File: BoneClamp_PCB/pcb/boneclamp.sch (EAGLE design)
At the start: 4 parts, among them U1 AD7656YSTZ, U2 AD5754RBREZ, U3 SN74ABT541BDW

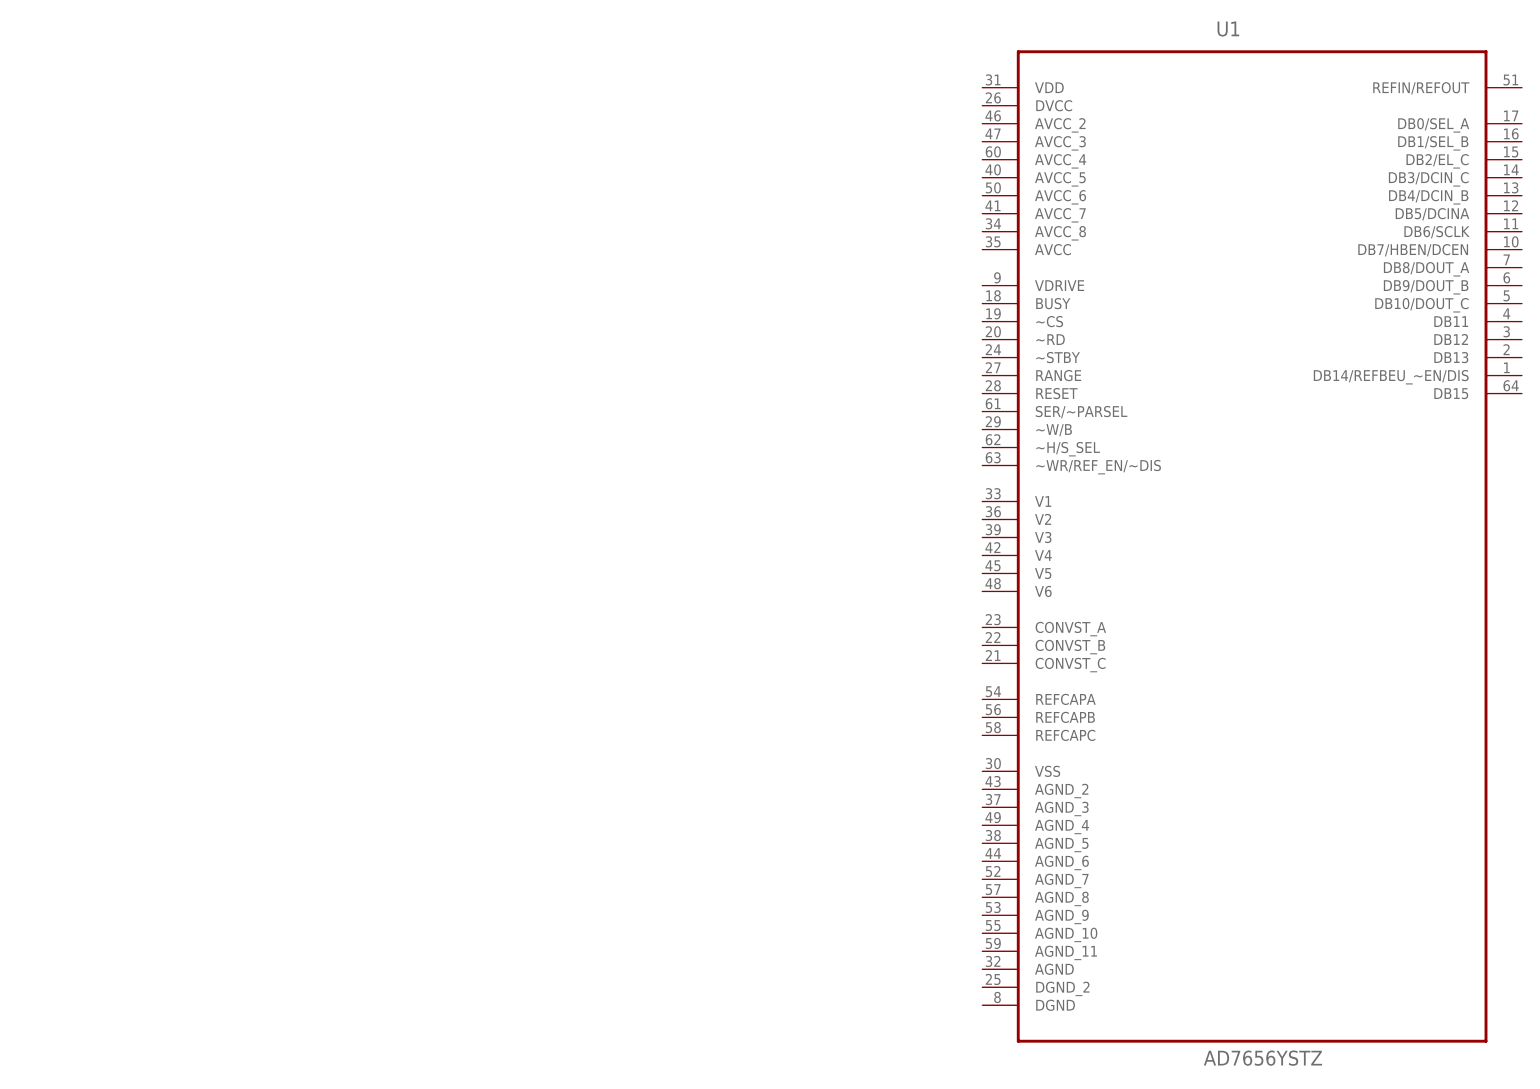
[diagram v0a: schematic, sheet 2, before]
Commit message: Updated schematic with the TRS jacks that we will use. They are mono which makes conversion to BNC or other formats easy. Also, I added a .gitignore to the main BoneClamp folder so that we can avoid committing executables and backup files.
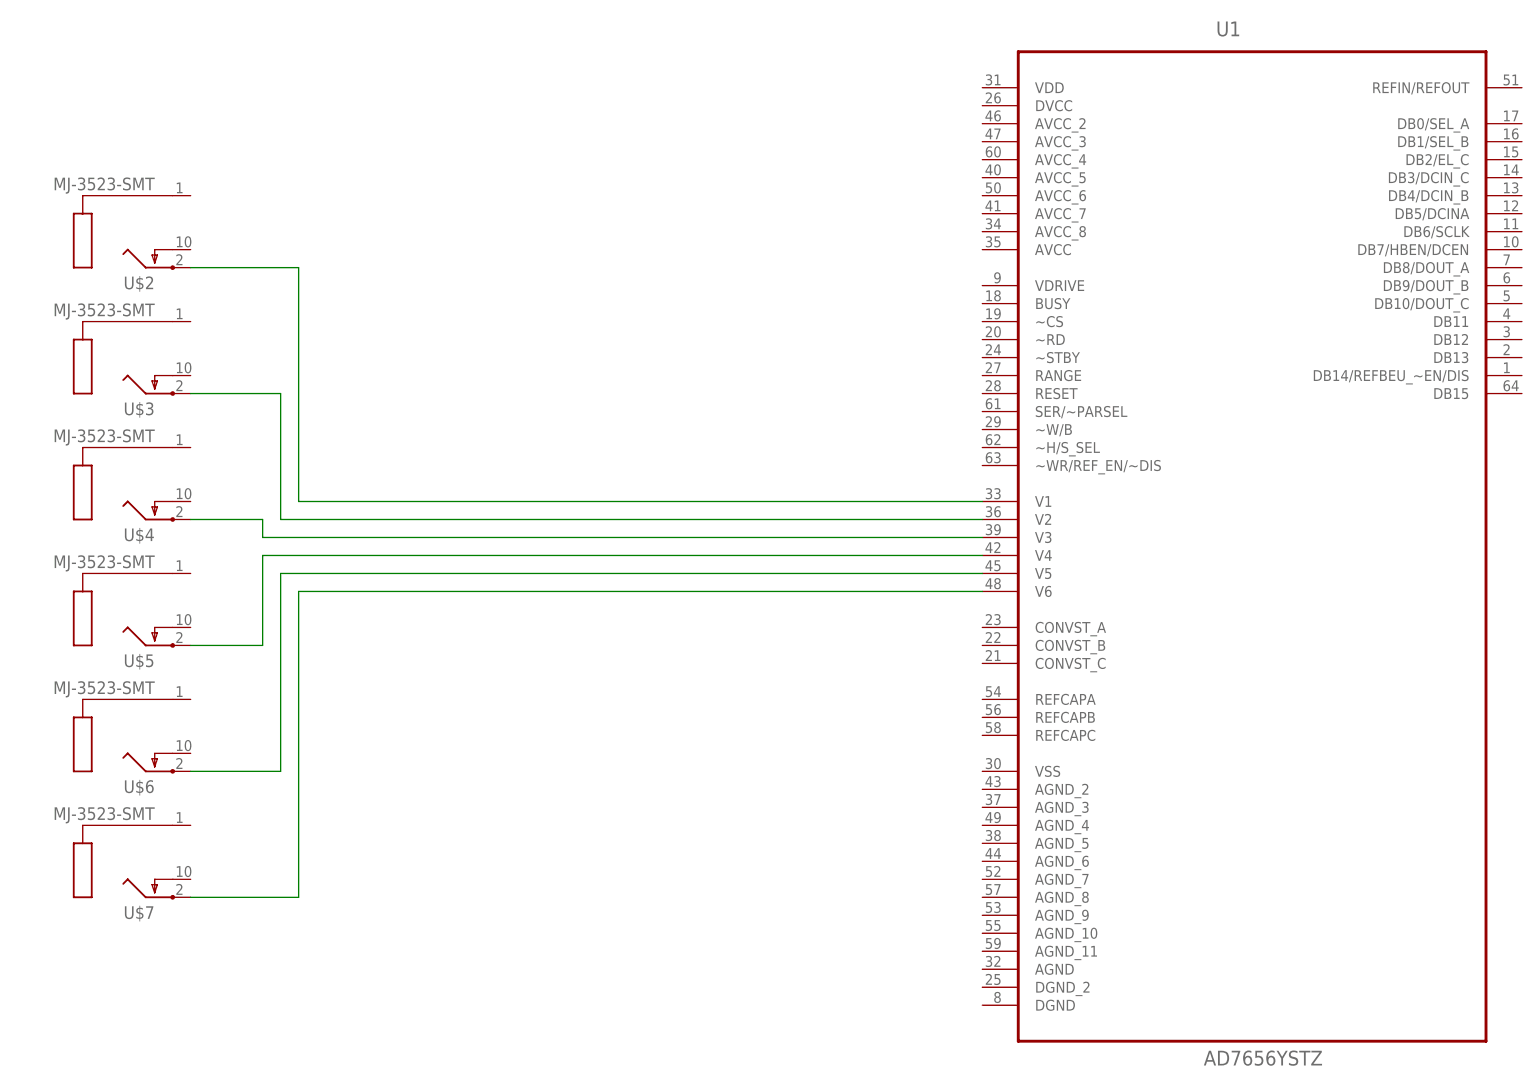
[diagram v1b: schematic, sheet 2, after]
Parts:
- added U$10, U$11, U$12, U$2, U$3, U$4, U$5, U$6, U$7, U$8: MJ-3523-SMT, con-cuistack:MJ-3523-SMT
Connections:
- new net N$1: U$6.TIP, U1.V5
- new net N$11: U$12.TIP, U2.VOUTD
- new net N$2: U$7.TIP, U1.V6
- new net N$3: U$5.TIP, U1.V4
- new net N$4: U$4.TIP, U1.V3
- new net N$5: U$3.TIP, U1.V2
- new net N$6: U$2.TIP, U1.V1
- new net N$7: U$8.TIP, U2.VOUTA
- new net N$8: U$10.TIP, U2.VOUTB
- new net N$9: U$11.TIP, U2.VOUTC
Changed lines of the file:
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@@
 <part name="U2" library="analog-devices-01" deviceset="AD5754RBREZ" device=""/>
 <part name="U3" library="ti-extended" deviceset="SN74ABT541BDW" device=""/>
+<part name="U$2" library="con-cuistack" deviceset="MJ-3523-SMT" device=""/>
+<part name="U$3" library="con-cuistack" deviceset="MJ-3523-SMT" device=""/>
+<part name="U$4" library="con-cuistack" deviceset="MJ-3523-SMT" device=""/>
+<part name="U$5" library="con-cuistack" deviceset="MJ-3523-SMT" device=""/>
+<part name="U$6" library="con-cuistack" deviceset="MJ-3523-SMT" device=""/>
+<part name="U$7" library="con-cuistack" deviceset="MJ-3523-SMT" device=""/>
+<part name="U$10" library="con-cuistack" deviceset="MJ-3523-SMT" device=""/>
+<part name="U$11" library="con-cuistack" deviceset="MJ-3523-SMT" device=""/>
+<part name="U$12" library="con-cuistack" deviceset="MJ-3523-SMT" device=""/>
+<part name="U$8" library="con-cuistack" deviceset="MJ-3523-SMT" device=""/>
 </parts>
 <sheets>
@@
 <instances>
 <instance part="U1" gate="A" x="76.2" y="35.56"/>
+<instance part="U$2" gate="G$1" x="-81.28" y="76.2" rot="R180"/>
+<instance part="U$3" gate="G$1" x="-81.28" y="58.42" rot="R180"/>
+<instance part="U$4" gate="G$1" x="-81.28" y="40.64" rot="R180"/>
+<instance part="U$5" gate="G$1" x="-81.28" y="22.86" rot="R180"/>
+<instance part="U$6" gate="G$1" x="-81.28" y="5.08" rot="R180"/>
+<instance part="U$7" gate="G$1" x="-81.28" y="-12.7" rot="R180"/>
 </instances>
 <busses>
 </busses>
 <nets>
+<net name="N$3" class="0">
+<segment>
+<pinref part="U1" gate="A" pin="V4"/>
+<wire x1="-63.5" y1="30.48" x2="38.1" y2="30.48" width="0.1524" layer="91"/>
+<wire x1="-63.5" y1="30.48" x2="-63.5" y2="17.78" width="0.1524" layer="91"/>
+<pinref part="U$5" gate="G$1" pin="TIP"/>
+<wire x1="-63.5" y1="17.78" x2="-73.66" y2="17.78" width="0.1524" layer="91"/>
+</segment>
+</net>
+<net name="N$4" class="0">
+<segment>
+<wire x1="-63.5" y1="35.56" x2="-63.5" y2="33.02" width="0.1524" layer="91"/>
+<pinref part="U1" gate="A" pin="V3"/>
+<wire x1="-63.5" y1="33.02" x2="38.1" y2="33.02" width="0.1524" layer="91"/>
+<pinref part="U$4" gate="G$1" pin="TIP"/>
+<wire x1="-73.66" y1="35.56" x2="-63.5" y2="35.56" width="0.1524" layer="91"/>
+</segment>
+</net>
+<net name="N$5" class="0">
+<segment>
+<pinref part="U1" gate="A" pin="V2"/>
+<wire x1="38.1" y1="35.56" x2="-60.96" y2="35.56" width="0.1524" layer="91"/>
+<wire x1="-60.96" y1="35.56" x2="-60.96" y2="53.34" width="0.1524" layer="91"/>
+<pinref part="U$3" gate="G$1" pin="TIP"/>
+<wire x1="-60.96" y1="53.34" x2="-73.66" y2="53.34" width="0.1524" layer="91"/>
+</segment>
+</net>
+<net name="N$6" class="0">
+<segment>
+<wire x1="-58.42" y1="71.12" x2="-58.42" y2="38.1" width="0.1524" layer="91"/>
+<pinref part="U1" gate="A" pin="V1"/>
+<wire x1="-58.42" y1="38.1" x2="38.1" y2="38.1" width="0.1524" layer="91"/>
+<pinref part="U$2" gate="G$1" pin="TIP"/>
+<wire x1="-73.66" y1="71.12" x2="-58.42" y2="71.12" width="0.1524" layer="91"/>
+</segment>
+</net>
+<net name="N$1" class="0">
+<segment>
+<pinref part="U1" gate="A" pin="V5"/>
+<wire x1="-60.96" y1="27.94" x2="38.1" y2="27.94" width="0.1524" layer="91"/>
+<wire x1="-60.96" y1="27.94" x2="-60.96" y2="0" width="0.1524" layer="91"/>
+<pinref part="U$6" gate="G$1" pin="TIP"/>
+<wire x1="-60.96" y1="0" x2="-73.66" y2="0" width="0.1524" layer="91"/>
+</segment>
+</net>
+<net name="N$2" class="0">
+<segment>
+<pinref part="U1" gate="A" pin="V6"/>
+<wire x1="-58.42" y1="25.4" x2="38.1" y2="25.4" width="0.1524" layer="91"/>
+<wire x1="-58.42" y1="25.4" x2="-58.42" y2="-17.78" width="0.1524" layer="91"/>
+<pinref part="U$7" gate="G$1" pin="TIP"/>
+<wire x1="-58.42" y1="-17.78" x2="-73.66" y2="-17.78" width="0.1524" layer="91"/>
+</segment>
+</net>
 </nets>
 </sheet>
@@
 <instances>
 <instance part="U2" gate="A" x="73.66" y="50.8"/>
+<instance part="U$10" gate="G$1" x="177.8" y="63.5"/>
+<instance part="U$11" gate="G$1" x="177.8" y="45.72"/>
+<instance part="U$12" gate="G$1" x="177.8" y="27.94"/>
+<instance part="U$8" gate="G$1" x="177.8" y="81.28"/>
 </instances>
 <busses>
 </busses>
 <nets>
+<net name="N$7" class="0">
+<segment>
+<pinref part="U2" gate="A" pin="VOUTA"/>
+<wire x1="93.98" y1="78.74" x2="152.4" y2="78.74" width="0.1524" layer="91"/>
+<wire x1="152.4" y1="78.74" x2="152.4" y2="86.36" width="0.1524" layer="91"/>
+<pinref part="U$8" gate="G$1" pin="TIP"/>
+<wire x1="152.4" y1="86.36" x2="170.18" y2="86.36" width="0.1524" layer="91"/>
+</segment>
+</net>
+<net name="N$8" class="0">
+<segment>
+<pinref part="U2" gate="A" pin="VOUTB"/>
+<wire x1="152.4" y1="76.2" x2="93.98" y2="76.2" width="0.1524" layer="91"/>
+<wire x1="152.4" y1="76.2" x2="152.4" y2="68.58" width="0.1524" layer="91"/>
+<pinref part="U$10" gate="G$1" pin="TIP"/>
+<wire x1="152.4" y1="68.58" x2="170.18" y2="68.58" width="0.1524" layer="91"/>
+</segment>
+</net>
+<net name="N$9" class="0">
+<segment>
+<pinref part="U2" gate="A" pin="VOUTC"/>
+<wire x1="93.98" y1="73.66" x2="149.86" y2="73.66" width="0.1524" layer="91"/>
+<wire x1="149.86" y1="73.66" x2="149.86" y2="50.8" width="0.1524" layer="91"/>
+<pinref part="U$11" gate="G$1" pin="TIP"/>
+<wire x1="149.86" y1="50.8" x2="170.18" y2="50.8" width="0.1524" layer="91"/>
+</segment>
+</net>
+<net name="N$11" class="0">
+<segment>
+<pinref part="U2" gate="A" pin="VOUTD"/>
+<wire x1="93.98" y1="71.12" x2="147.32" y2="71.12" width="0.1524" layer="91"/>
+<wire x1="147.32" y1="71.12" x2="147.32" y2="33.02" width="0.1524" layer="91"/>
+<pinref part="U$12" gate="G$1" pin="TIP"/>
+<wire x1="147.32" y1="33.02" x2="170.18" y2="33.02" width="0.1524" layer="91"/>
+</segment>
+</net>
 </nets>
 </sheet>

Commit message: Updated the adafruit libary to include the d-sub connector we will be using. Updated .gitignore to ingore libary backups. Started a power supply sheet on the eagle schematic.
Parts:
- removed U$10, U$11, U$12, U$2, U$3, U$4, U$5, U$6, U$7, U$8: MJ-3523-SMT, con-cuistack:MJ-3523-SMT
- added C2: (no value), rcl:C-EUC0603
- added JP1: (no value), jumper:JP1E
- added SJ1, SJ2, SJ3: (no value), jumper:SJ
- added X1: F15-SHEILD, adafruit:F15-SHEILD
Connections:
- removed net N$11: U$12.TIP, U2.VOUTD
- removed net N$9: U$11.TIP, U2.VOUTC
- new net AGND: JP1.2, X1.1
- new net DAC_A: U2.VOUTA, X1.8
- new net DAC_B: U2.VOUTB, X1.9
- new net DAC_C: U2.VOUTC, X1.10
- new net DAC_D: U2.VOUTD, X1.11
- new net SDIN_BB: SJ2.1
- new net SDIN_DC: SJ3.1
- new net SDO_DC: SJ1.2
- new net SGND: JP1.1, X1.P$1, X1.P$2
- net N$1: now also U1.V1, X1.2; no longer U$6.TIP, U1.V5
- net N$2: now also U1.V2, X1.3; no longer U$7.TIP, U1.V6
- net N$3: now also U1.V3, X1.4; no longer U$5.TIP, U1.V4
- net N$4: now also U1.V4, X1.5; no longer U$4.TIP, U1.V3
- net N$5: now also U1.V5, X1.6; no longer U$3.TIP, U1.V2
- net N$6: now also U1.V6, X1.7; no longer U$2.TIP, U1.V1
- net N$7: now also SJ1.1, U2.SDO; no longer U$8.TIP, U2.VOUTA
- net N$8: now also SJ2.2, SJ3.2, U2.SDIN; no longer U$10.TIP, U2.VOUTB
